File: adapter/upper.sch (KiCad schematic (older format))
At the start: 9 parts, among them J11 MALE, J12 FEMALE, J13 STANDOFF, J14 STANDOFF, J15 STANDOFF

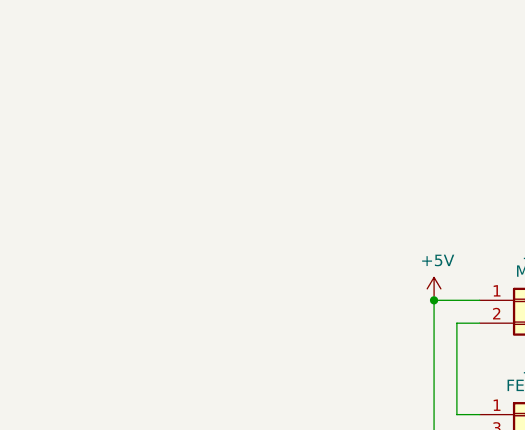
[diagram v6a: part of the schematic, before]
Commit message: Add power flags to pass DRC check
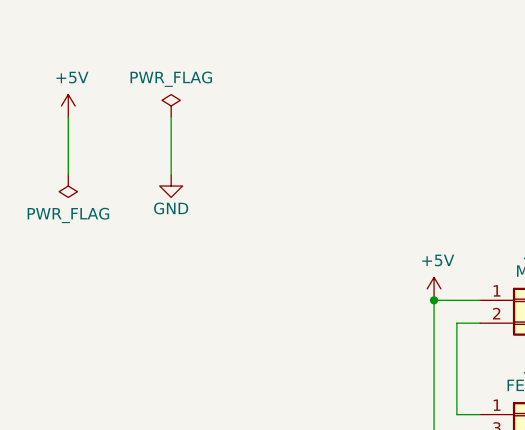
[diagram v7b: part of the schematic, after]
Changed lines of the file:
@@
 P 7250 3000
 AR Path="/5FA6C89B/5FC055F4" Ref="#PWR?"  Part="1"
-AR Path="/5FA6C6C8/5FC055F4" Ref="#PWR?"  Part="1"
-F 0 "#PWR?" H 7250 2850 50  0001 C CNN
+AR Path="/5FA6C6C8/5FC055F4" Ref="#PWR0102"  Part="1"
+F 0 "#PWR0102" H 7250 2850 50  0001 C CNN
 F 1 "+5V" H 7265 3173 50  0000 C CNN
 F 2 "" H 7250 3000 50  0001 C CNN
@@
 Wire Wire Line
 	7250 3000 8500 3000
+$Comp
+L power:PWR_FLAG #FLG?
+U 1 1 5FC09A46
+P 4000 2100
+AR Path="/5FA6C89B/5FC09A46" Ref="#FLG?"  Part="1"
+AR Path="/5FA6C6C8/5FC09A46" Ref="#FLG0103"  Part="1"
+F 0 "#FLG0103" H 4000 2175 50  0001 C CNN
+F 1 "PWR_FLAG" H 4000 2273 50  0000 C CNN
+F 2 "" H 4000 2100 50  0001 C CNN
+F 3 "~" H 4000 2100 50  0001 C CNN
+	1    4000 2100
+	1    0    0    -1
+$EndComp
+$Comp
+L power:PWR_FLAG #FLG?
+U 1 1 5FC09A4C
+P 3550 2350
+AR Path="/5FA6C89B/5FC09A4C" Ref="#FLG?"  Part="1"
+AR Path="/5FA6C6C8/5FC09A4C" Ref="#FLG0104"  Part="1"
+F 0 "#FLG0104" H 3550 2425 50  0001 C CNN
+F 1 "PWR_FLAG" H 3550 2523 50  0000 C CNN
+F 2 "" H 3550 2350 50  0001 C CNN
+F 3 "~" H 3550 2350 50  0001 C CNN
+	1    3550 2350
+	-1   0    0    1
+$EndComp
+Wire Wire Line
+	4000 2100 4000 2350
+Wire Wire Line
+	3550 2100 3550 2350
+$Comp
+L power:+5V #PWR?
+U 1 1 5FC09CB6
+P 3550 2100
+AR Path="/5FA6C89B/5FC09CB6" Ref="#PWR?"  Part="1"
+AR Path="/5FA6C6C8/5FC09CB6" Ref="#PWR0103"  Part="1"
+F 0 "#PWR0103" H 3550 1950 50  0001 C CNN
+F 1 "+5V" H 3565 2273 50  0000 C CNN
+F 2 "" H 3550 2100 50  0001 C CNN
+F 3 "" H 3550 2100 50  0001 C CNN
+	1    3550 2100
+	1    0    0    -1
+$EndComp
+$Comp
+L power:GND #PWR?
+U 1 1 5FC09E08
+P 4000 2350
+AR Path="/5FA6C89B/5FC09E08" Ref="#PWR?"  Part="1"
+AR Path="/5FA6C6C8/5FC09E08" Ref="#PWR0104"  Part="1"
+F 0 "#PWR0104" H 4000 2100 50  0001 C CNN
+F 1 "GND" H 4000 2200 50  0000 C CNN
+F 2 "" H 4000 2350 50  0001 C CNN
+F 3 "" H 4000 2350 50  0001 C CNN
+	1    4000 2350
+	1    0    0    -1
+$EndComp
 $EndSCHEMATC

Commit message: Fix pinout
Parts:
- added J13: MALE, Connector_PinHeader_2.54mm:PinHeader_2x02_P2.54mm_Horizontal, symbol Connector_Generic:Conn_02x02_Top_Bottom
- renumbered J13 to J14, J14 to J15, J15 to J16
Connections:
- net +5V: now also J13.4 (Pin_4)
- net GND: now also J13.2 (Pin_2)
- net at J11.2 (Pin_2), J12.1 (Pin_1): now also J13.3 (Pin_3)
- net at J11.4 (Pin_4), J12.2 (Pin_2): now also J13.1 (Pin_1)
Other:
- moved on the sheet: J12
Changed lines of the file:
@@
 	5350 2900 5150 2900
 Wire Wire Line
-	5150 2900 5150 3500
-Wire Wire Line
-	6050 3500 6050 3550
+	6050 4000 6050 4050
 Wire Wire Line
 	5850 3000 5950 3000
@@
 L power:GND #PWR?
 U 1 1 5FB6CCB9
-P 6050 3550
+P 6050 4050
 AR Path="/5FA6C89B/5FB6CCB9" Ref="#PWR?"  Part="1"
 AR Path="/5FA6C6C8/5FB6CCB9" Ref="#PWR0111"  Part="1"
-F 0 "#PWR0111" H 6050 3300 50  0001 C CNN
-F 1 "GND" H 6050 3400 50  0000 C CNN
-F 2 "" H 6050 3550 50  0001 C CNN
-F 3 "" H 6050 3550 50  0001 C CNN
-	1    6050 3550
+F 0 "#PWR0111" H 6050 3800 50  0001 C CNN
+F 1 "GND" H 6050 3900 50  0000 C CNN
+F 2 "" H 6050 4050 50  0001 C CNN
+F 3 "" H 6050 4050 50  0001 C CNN
+	1    6050 4050
 	1    0    0    -1
 $EndComp
@@
 L Connector_Generic:Conn_02x02_Odd_Even J?
 U 1 1 5FB6CCC7
-P 5550 3400
+P 5550 3900
 AR Path="/5FB6CCC7" Ref="J?"  Part="1"
 AR Path="/5FA6C89B/5FB6CCC7" Ref="J?"  Part="1"
 AR Path="/5FA6C6C8/5FB6CCC7" Ref="J12"  Part="1"
-F 0 "J12" H 5600 3617 50  0000 C CNN
-F 1 "FEMALE" H 5600 3526 50  0000 C CNN
-F 2 "Connector_PinSocket_2.54mm:PinSocket_2x02_P2.54mm_Horizontal" H 5550 3400 50  0001 C CNN
-F 3 "~" H 5550 3400 50  0001 C CNN
-	1    5550 3400
-	1    0    0    -1
-$EndComp
-Wire Wire Line
-	5850 3500 6050 3500
-Wire Wire Line
-	5850 3400 5950 3400
-Wire Wire Line
-	5950 3000 5950 3400
+F 0 "J12" H 5600 4117 50  0000 C CNN
+F 1 "FEMALE" H 5600 4026 50  0000 C CNN
+F 2 "Connector_PinSocket_2.54mm:PinSocket_2x02_P2.54mm_Horizontal" H 5550 3900 50  0001 C CNN
+F 3 "~" H 5550 3900 50  0001 C CNN
+	1    5550 3900
+	1    0    0    -1
+$EndComp
+Wire Wire Line
+	5850 4000 6050 4000
+Wire Wire Line
+	5850 3900 5950 3900
 Wire Wire Line
 	5850 2900 6050 2900
-Wire Wire Line
-	6050 2900 6050 3500
-Connection ~ 6050 3500
+Connection ~ 6050 4000
 Connection ~ 5150 2900
 Wire Wire Line
 	5350 3000 5250 3000
 Wire Wire Line
-	5150 3500 5350 3500
-Wire Wire Line
-	5250 3000 5250 3400
-Wire Wire Line
-	5250 3400 5350 3400
+	5150 4000 5350 4000
+Wire Wire Line
+	5250 3900 5350 3900
 $Comp
 L Connector_Generic:Conn_01x01 J?
@@
 P 8700 2000
 AR Path="/5FA6C89B/5FB93146" Ref="J?"  Part="1"
-AR Path="/5FA6C6C8/5FB93146" Ref="J13"  Part="1"
-F 0 "J13" H 8780 2042 50  0000 L CNN
+AR Path="/5FA6C6C8/5FB93146" Ref="J14"  Part="1"
+F 0 "J14" H 8780 2042 50  0000 L CNN
 F 1 "STANDOFF" H 8780 1951 50  0000 L CNN
 F 2 "MountingHole:MountingHole_2.2mm_M2_Pad_Via" H 8700 2000 50  0001 C CNN
@@
 P 8700 2500
 AR Path="/5FA6C89B/5FB9314D" Ref="J?"  Part="1"
-AR Path="/5FA6C6C8/5FB9314D" Ref="J14"  Part="1"
-F 0 "J14" H 8780 2542 50  0000 L CNN
+AR Path="/5FA6C6C8/5FB9314D" Ref="J15"  Part="1"
+F 0 "J15" H 8780 2542 50  0000 L CNN
 F 1 "STANDOFF" H 8780 2451 50  0000 L CNN
 F 2 "MountingHole:MountingHole_2.2mm_M2_Pad_Via" H 8700 2500 50  0001 C CNN
@@
 P 8700 3000
 AR Path="/5FA6C89B/5FB93153" Ref="J?"  Part="1"
-AR Path="/5FA6C6C8/5FB93153" Ref="J15"  Part="1"
-F 0 "J15" H 8780 3042 50  0000 L CNN
+AR Path="/5FA6C6C8/5FB93153" Ref="J16"  Part="1"
+F 0 "J16" H 8780 3042 50  0000 L CNN
 F 1 "STANDOFF" H 8780 2951 50  0000 L CNN
 F 2 "MountingHole:MountingHole_2.2mm_M2_Pad_Via" H 8700 3000 50  0001 C CNN
@@
 	1    0    0    -1
 $EndComp
+$Comp
+L Connector_Generic:Conn_02x02_Top_Bottom J?
+U 1 1 5FCC3ECF
+P 5650 3500
+AR Path="/5FCC3ECF" Ref="J?"  Part="1"
+AR Path="/5FA6C89B/5FCC3ECF" Ref="J?"  Part="1"
+AR Path="/5FA6C6C8/5FCC3ECF" Ref="J13"  Part="1"
+F 0 "J13" H 5700 3717 50  0000 C CNN
+F 1 "MALE" H 5700 3626 50  0000 C CNN
+F 2 "Connector_PinHeader_2.54mm:PinHeader_2x02_P2.54mm_Horizontal" H 5650 3500 50  0001 C CNN
+F 3 "~" H 5650 3500 50  0001 C CNN
+	1    5650 3500
+	-1   0    0    1
+$EndComp
+Wire Wire Line
+	5350 3400 5150 3400
+Wire Wire Line
+	5150 2900 5150 3400
+Wire Wire Line
+	5150 3400 5150 4000
+Connection ~ 5150 3400
+Wire Wire Line
+	5350 3500 5250 3500
+Wire Wire Line
+	5250 3000 5250 3500
+Wire Wire Line
+	5250 3500 5250 3900
+Connection ~ 5250 3500
+Wire Wire Line
+	5850 3400 6050 3400
+Wire Wire Line
+	6050 2900 6050 3400
+Wire Wire Line
+	6050 3400 6050 4000
+Connection ~ 6050 3400
+Wire Wire Line
+	5850 3500 5950 3500
+Wire Wire Line
+	5950 3000 5950 3500
+Wire Wire Line
+	5950 3500 5950 3900
+Connection ~ 5950 3500
 $EndSCHEMATC
